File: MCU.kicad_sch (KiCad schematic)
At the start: 25 parts, among them J1 Conn_01x06_Pin, J2 Conn_01x03, SW1 SW_MEC_5E, U2 STM32H503RBTx, Y1 Crystal

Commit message: Wip
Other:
- note added: "Pin number: 13(3)/64"

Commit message: wip
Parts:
- removed R11: R, Resistor_SMD:R_0805_2012Metric_Pad1.20x1.40mm_HandSolder, symbol Device:R
- removed U2: STM32H503RBTx, Package_QFP:LQFP-64_10x10mm_P0.5mm, symbol Stm32h503rbt6:STM32H503RBTx
- added U6: STM32H523RCTx, Package_QFP:LQFP-64_10x10mm_P0.5mm, symbol MCU_ST_STM32H5:STM32H523RCTx
- C1: value C -> 100n
- R10, R4, R5, R6, R7, R9: value R -> 50
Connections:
- net +3.3V: now also U6.1 (VBAT), U6.19 (VDD), U6.32 (VDD), U6.48 (VDD), U6.64 (VDD)
- net Boot: now also U6.60 (BOOT0)
- net BusVoltage: now also U6.11 (PC3)
- net CH1: now also R6.1, U6.41 (PA8)
- net CH1N: now also R10.1, U6.34 (PB13)
- net CH2: now also R5.1, U6.42 (PA9)
- net CH2N: now also R9.1, U6.35 (PB14)
- net CH3: now also R4.1, U6.43 (PA10)
- net CH3N: now also R7.2, U6.36 (PB15)
- net Current_A: now also U6.17 (PA3)
- net Current_B: now also U6.16 (PA2)
- net Current_C: now also U6.15 (PA1)
- net Encoder_0: now also U6.54 (PD2)
- net Encoder_A: now also U6.21 (PA5), U6.22 (PA6)
- net Encoder_B: now also U6.23 (PA7), U6.24 (PC4)
- net MISO: now also U6.26 (PB0)
- net MOSI: now also U6.28 (PB2)
- net NRST: now also U6.7 (NRST)
- net RCC_In: now also U6.5 (PH0)
- net RCC_Out: now also U6.6 (PH1)
- net SCLK: now also U6.27 (PB1)
- net SWCLK: now also U6.49 (PA14(JTCK)
- net SWDIO: now also U6.46 (PA13(JTMS)
- net SWO: now also U6.55 (PB3(JTDO)
- net Vcap1: now also U6.30 (VCAP)
- net Vcap2: now also U6.62 (VCAP)
- net heatsinkTemperature: now also U6.14 (PA0)
- net nCS: now also U6.29 (PB10)
- net PWM_AL: now reaches R10.2
- net PWM_BH: now reaches R5.2
- net PWM_BL: now reaches R9.2
- net PWM_CL: now reaches R7.1
- net PWM_CH: now reaches R4.2
- net PWM_AH: now reaches R6.2
- new net: U6.18 (VSS), U6.31 (VSS), U6.47 (VSS), U6.63 (VSS)
- new net Disable_Drive: U6.44 (PA11)

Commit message: wip
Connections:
- net GNDD: now also U6.12 (VSSA), U6.18 (VSS), U6.31 (VSS), U6.47 (VSS), U6.63 (VSS)
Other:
- note removed: "Add connector for user panel"
- moved on the sheet: R10, R4, R5, R6, R7, R9

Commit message: 90% schematic first layout
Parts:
- removed SW1: SW_MEC_5E, Button_Switch_SMD:SW_MEC_5GSH9, symbol Switch:SW_MEC_5E
- removed Y1: Crystal, Crystal:Crystal_SMD_HC49-SD, symbol Device:Crystal
- added R31, R32, R33, R34: 50, Resistor_SMD:R_0805_2012Metric_Pad1.20x1.40mm_HandSolder, symbol Device:R
- added SW1: SW_Push, Button_Switch_THT:SW_PUSH_6mm_H5mm, symbol Switch:SW_Push
- added U7: CSTNE8M00G550000R0, CSTNE16M0V530000R0, symbol CSTNE8M00G550000R0:CSTNE8M00G550000R0
- R1: value R -> 10k
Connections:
- net GNDD: now also SW1.1, U7.2 (GND)
- net MISO: now also R31.1, R31.2
- net MOSI: now also R33.1, R33.2
- net NRST: now also SW1.2
- net RCC_In: now also U7.1 (INPUT)
- net RCC_Out: now also U7.3 (OUTPUT)
- net SCLK: now also R32.1, R32.2
- net nCS: now also R34.1, R34.2
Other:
- note added: "Pin number: 8(3)/64"
- note removed: "Pin number: 13(3)/64"
- moved on the sheet: C10, C9

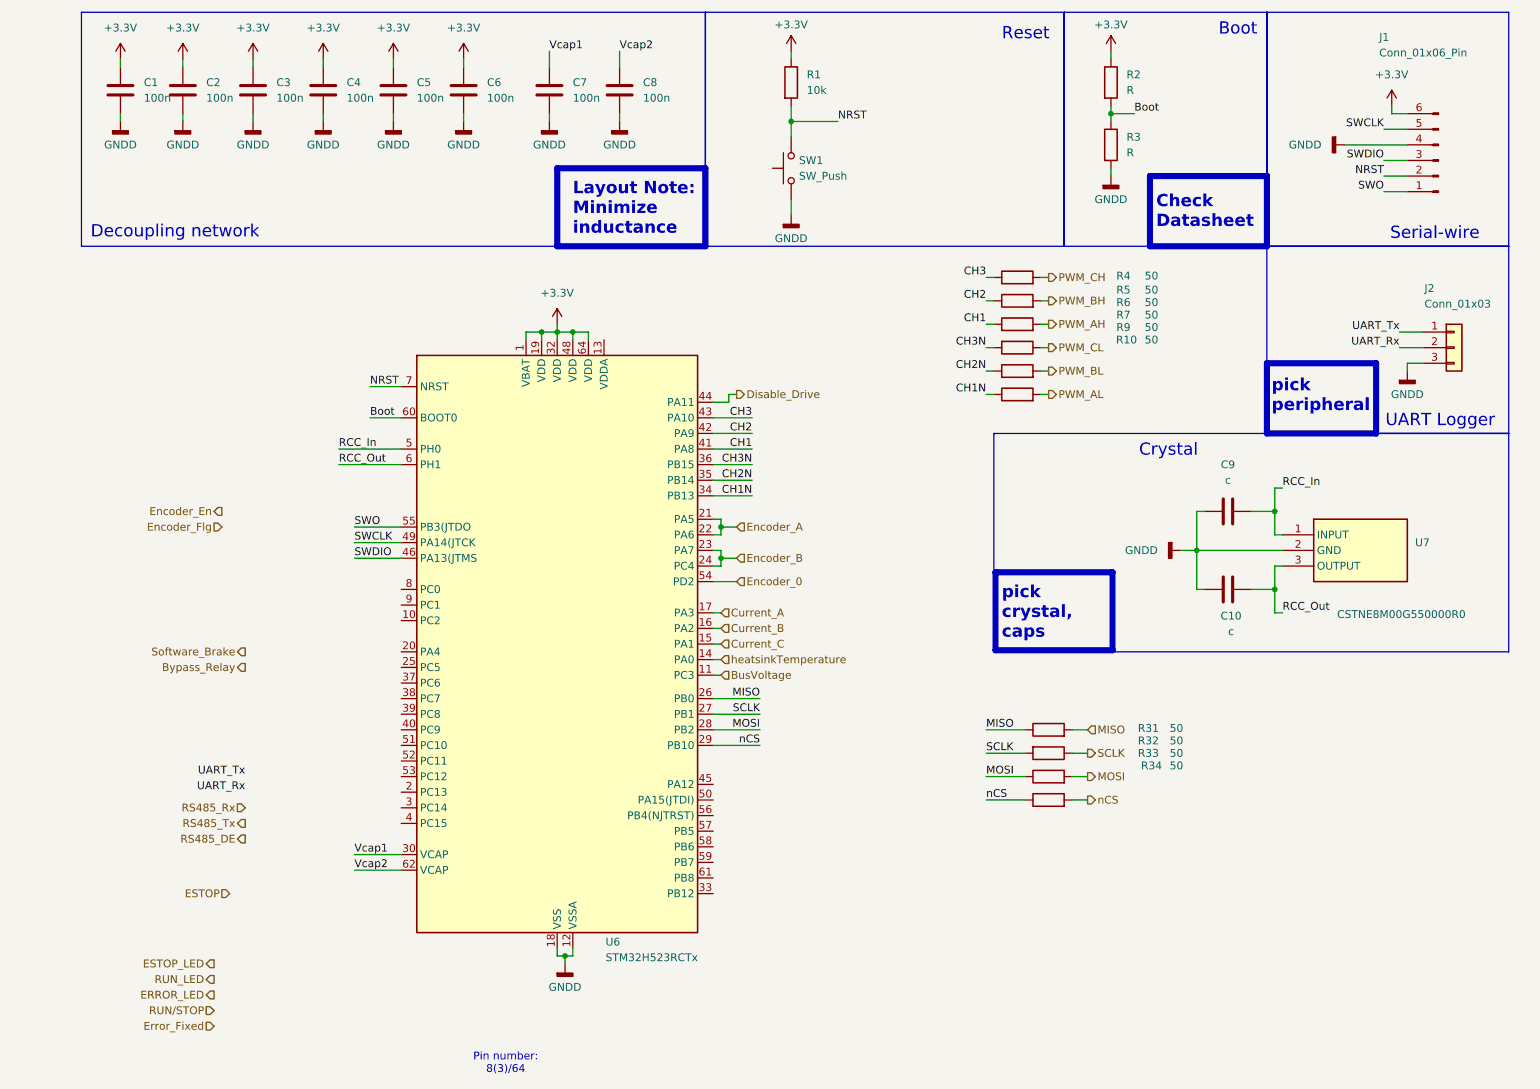
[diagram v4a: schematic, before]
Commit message: Addition of testpoints
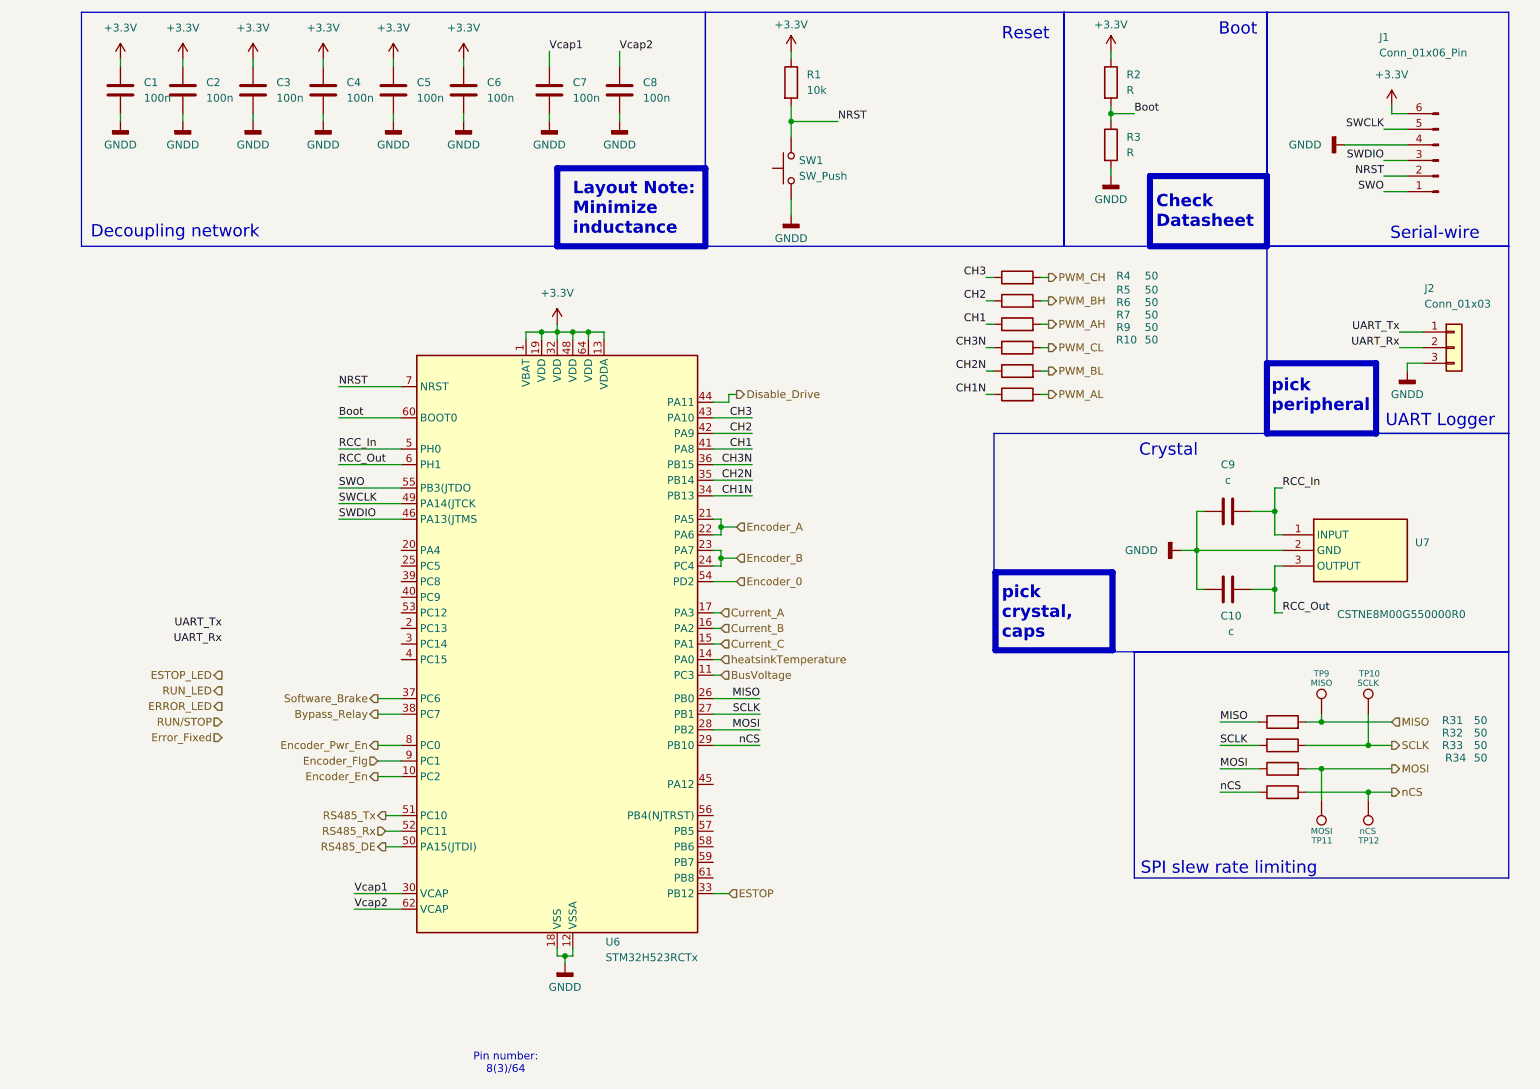
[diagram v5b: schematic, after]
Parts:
- added TP10: SCLK, TestPoint:TestPoint_Pad_D1.0mm, symbol Connector:TestPoint
- added TP11: MOSI, TestPoint:TestPoint_Pad_D1.0mm, symbol Connector:TestPoint
- added TP12: nCS, TestPoint:TestPoint_Pad_D1.0mm, symbol Connector:TestPoint
- added TP9: MISO, TestPoint:TestPoint_Pad_D1.0mm, symbol Connector:TestPoint
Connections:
- net +3.3V: now also U6.13 (VDDA)
- net Bypass_Relay: now also U6.38 (PC7)
- net ESTOP: now also U6.33 (PB12)
- net Encoder_En: now also U6.10 (PC2)
- net Encoder_Flg: now also U6.9 (PC1)
- net MISO: now also TP9.1
- net MOSI: now also TP11.1
- net RS485_DE: now also U6.50 (PA15(JTDI))
- net RS485_Rx: now also U6.52 (PC11)
- net RS485_Tx: now also U6.51 (PC10)
- net SCLK: now also TP10.1
- net Software_Brake: now also U6.37 (PC6)
- net nCS: now also TP12.1
- net Encoder_Pwr_En: now reaches U6.8 (PC0)
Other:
- note added: "SPI slew rate limiting"
- moved on the sheet: R31, R32, R33, R34
